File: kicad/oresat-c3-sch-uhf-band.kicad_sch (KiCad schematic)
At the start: 126 parts, among them Q3 NTR4101, Q4 PMV45EN, U16 AX5043, U18 LT5534, U19 BDCN-20-13+, U20 QPC1022, U21 TQP7M9105, U22 LT5534, U25 SN74LVC1G11IDCKRQ1, U26 TLV7041DBV, U27 LP2985AIM5-1.8_NOPB, U29 TQP3M9036, U32 SF2446E, U33 SF2446E, U40 MAX941EUA+, X1 TYKTBLSANF-16.000000

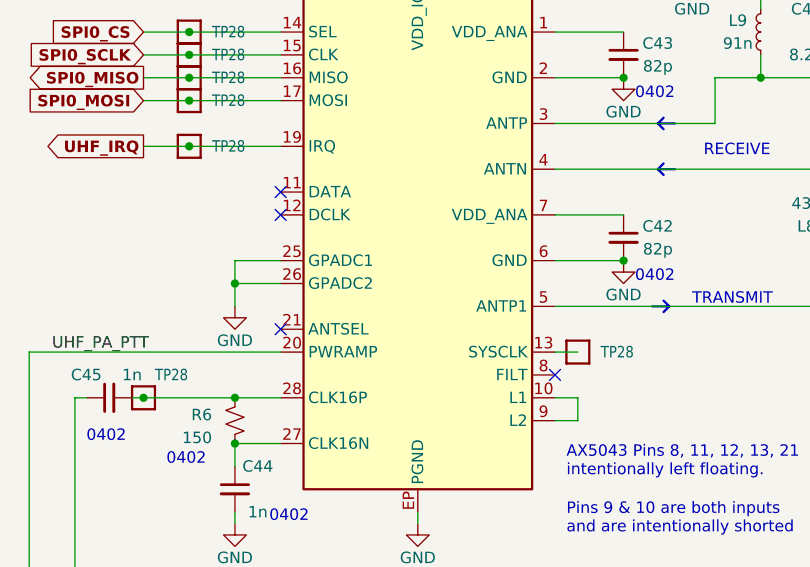
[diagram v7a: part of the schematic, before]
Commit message: Fixed some issues, including adding mrore capacitance. Also switched back to 0.38 mm for 50 ohm lines.
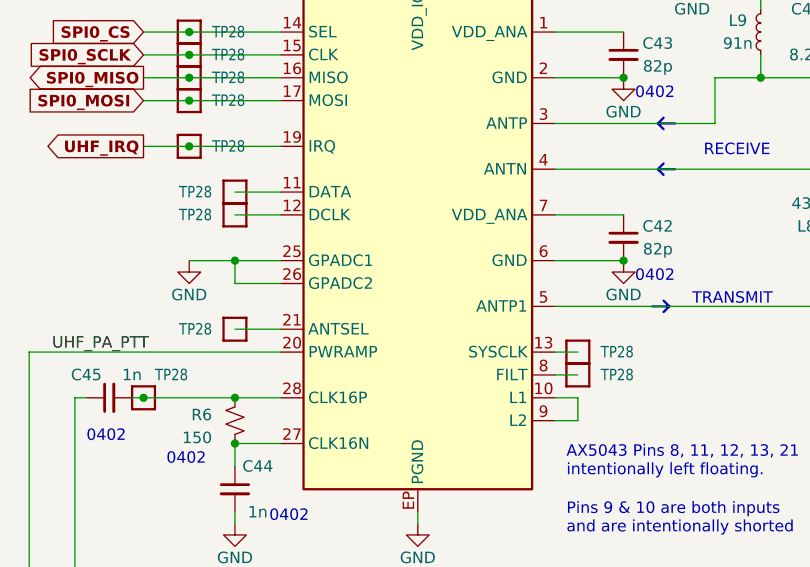
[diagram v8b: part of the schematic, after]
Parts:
- added TP28 (x4): Test-Point, oresat-misc:TestPoint_Pad_D1.0mm, symbol oresat-misc:Test-Point-1mm-round
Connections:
- net at U16.11 (DATA): now also TP28.1
- net at U16.12 (DCLK): now also TP28.1
- net at U16.21 (ANTSEL): now also TP28.1
- net at U16.8 (FILT): now also TP28.1
- no-connect marks 5 -> 1
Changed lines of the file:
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@@
   (junction (at 132.08 49.53) (diameter 0) (color 0 0 0 0)
   )
-  (junction (at 43.18 142.24) (diameter 0) (color 0 0 0 0)
-  )
   (junction (at 377.19 149.86) (diameter 0) (color 0 0 0 0)
   )
@@
   (junction (at 116.84 144.78) (diameter 0) (color 0 0 0 0)
   )
+  (junction (at 43.18 139.7) (diameter 0) (color 0 0 0 0)
+  )
   (junction (at 363.22 53.34) (diameter 0) (color 0 0 0 0)
   )
   (junction (at 38.1 119.38) (diameter 0) (color 0 0 0 0)
   )
-  (no_connect (at 48.26 132.08))
-  (no_connect (at 48.26 147.32))
-  (no_connect (at 48.26 134.62))
   (no_connect (at 30.48 215.9))
-  (no_connect (at 78.74 152.4))
   (wire (pts (xy 132.08 41.91) (xy 132.08 43.18))
     (stroke (width 0) (type default))
@@
     (stroke (width 0) (type default))
   )
+  (wire (pts (xy 43.18 132.08) (xy 48.26 132.08))
+    (stroke (width 0) (type default))
+  )
   (wire (pts (xy 96.52 48.26) (xy 96.52 46.99))
     (stroke (width 0) (type default))
@@
     (stroke (width 0) (type default))
   )
+  (wire (pts (xy 78.74 152.4) (xy 81.28 152.4))
+    (stroke (width 0) (type default))
+  )
   (wire (pts (xy 294.64 237.49) (xy 294.64 236.22))
     (stroke (width 0) (type default))
@@
     (stroke (width 0) (type default))
   )
-  (wire (pts (xy 43.18 144.78) (xy 43.18 142.24))
-    (stroke (width 0) (type default))
-  )
   (wire (pts (xy 81.28 204.47) (xy 66.04 204.47))
     (stroke (width 0) (type default))
@@
     (stroke (width 0) (type default))
   )
+  (wire (pts (xy 43.18 147.32) (xy 48.26 147.32))
+    (stroke (width 0) (type default))
+  )
   (wire (pts (xy 127 44.45) (xy 128.27 44.45))
     (stroke (width 0) (type default))
@@
     (stroke (width 0) (type default))
   )
+  (wire (pts (xy 38.1 139.7) (xy 43.18 139.7))
+    (stroke (width 0) (type default))
+  )
   (wire (pts (xy 335.28 59.69) (xy 335.28 60.96))
     (stroke (width 0) (type default))
@@
     (stroke (width 0) (type default))
   )
+  (wire (pts (xy 43.18 134.62) (xy 48.26 134.62))
+    (stroke (width 0) (type default))
+  )
   (wire (pts (xy 368.3 144.78) (xy 365.76 144.78))
     (stroke (width 0) (type default))
@@
     )
   )
+  (symbol (lib_id "oresat-misc:Test-Point-1mm-round") (at 43.18 147.32 270) (mirror x) (unit 1)
+    (in_bom yes) (on_board yes) (dnp no)
+    (property "Reference" "TP28" (at 40.64 147.3199 90)
+      (effects (font (size 1.27 1.0795)) (justify right))
+    )
+    (property "Value" "Test-Point" (at 50.8 147.32 0)
+      (effects (font (size 1.27 1.27)) hide)
+    )
+    (property "Footprint" "oresat-misc:TestPoint_Pad_D1.0mm" (at 53.34 147.32 0)
+      (effects (font (size 1.27 1.27)) hide)
+    )
+    (property "Datasheet" "" (at 43.18 147.32 0)
+      (effects (font (size 1.27 1.27)) hide)
+    )
+    (pin "1")
+    (instances
+      (project "oresat-c3"
+        (path "/65d12cdd-c326-4033-9053-c59fa4e0b25e/1b68ea4b-cacf-4529-b1d4-9be5d7c1043c"
+          (reference "TP28") (unit 1)
+        )
+        (path "/65d12cdd-c326-4033-9053-c59fa4e0b25e/05e45903-5042-4bc1-87af-e9d7510ea02d"
+          (reference "TP122") (unit 1)
+        )
+      )
+    )
+  )
   (symbol (lib_id "power:GND") (at 327.66 175.26 0) (mirror y) (unit 1)
     (in_bom yes) (on_board yes) (dnp no)
@@
     )
   )
+  (symbol (lib_id "oresat-misc:Test-Point-1mm-round") (at 43.18 134.62 270) (mirror x) (unit 1)
+    (in_bom yes) (on_board yes) (dnp no)
+    (property "Reference" "TP28" (at 40.64 134.6199 90)
+      (effects (font (size 1.27 1.0795)) (justify right))
+    )
+    (property "Value" "Test-Point" (at 50.8 134.62 0)
+      (effects (font (size 1.27 1.27)) hide)
+    )
+    (property "Footprint" "oresat-misc:TestPoint_Pad_D1.0mm" (at 53.34 134.62 0)
+      (effects (font (size 1.27 1.27)) hide)
+    )
+    (property "Datasheet" "" (at 43.18 134.62 0)
+      (effects (font (size 1.27 1.27)) hide)
+    )
+    (pin "1")
+    (instances
+      (project "oresat-c3"
+        (path "/65d12cdd-c326-4033-9053-c59fa4e0b25e/1b68ea4b-cacf-4529-b1d4-9be5d7c1043c"
+          (reference "TP28") (unit 1)
+        )
+        (path "/65d12cdd-c326-4033-9053-c59fa4e0b25e/05e45903-5042-4bc1-87af-e9d7510ea02d"
+          (reference "TP88") (unit 1)
+        )
+      )
+    )
+  )
   (symbol (lib_id "oresat-ics:AX5043") (at 63.5 137.16 0) (unit 1)
     (in_bom yes) (on_board yes) (dnp no) (fields_autoplaced)
@@
     )
   )
-  (symbol (lib_id "power:GND") (at 43.18 144.78 0) (mirror y) (unit 1)
+  (symbol (lib_id "power:GND") (at 38.1 139.7 0) (mirror y) (unit 1)
     (in_bom yes) (on_board yes) (dnp no)
-    (property "Reference" "#PWR0224" (at 43.18 151.13 0)
+    (property "Reference" "#PWR0224" (at 38.1 146.05 0)
       (effects (font (size 1.27 1.27)) hide)
     )
-    (property "Value" "GND" (at 43.18 148.59 0)
+    (property "Value" "GND" (at 38.1 143.51 0)
       (effects (font (size 1.27 1.27)))
     )
-    (property "Footprint" "" (at 43.18 144.78 0)
+    (property "Footprint" "" (at 38.1 139.7 0)
       (effects (font (size 1.27 1.27)) hide)
     )
-    (property "Datasheet" "" (at 43.18 144.78 0)
+    (property "Datasheet" "" (at 38.1 139.7 0)
       (effects (font (size 1.27 1.27)) hide)
     )
@@
     )
   )
+  (symbol (lib_id "oresat-misc:Test-Point-1mm-round") (at 43.18 132.08 270) (mirror x) (unit 1)
+    (in_bom yes) (on_board yes) (dnp no)
+    (property "Reference" "TP28" (at 40.64 132.0799 90)
+      (effects (font (size 1.27 1.0795)) (justify right))
+    )
+    (property "Value" "Test-Point" (at 50.8 132.08 0)
+      (effects (font (size 1.27 1.27)) hide)
+    )
+    (property "Footprint" "oresat-misc:TestPoint_Pad_D1.0mm" (at 53.34 132.08 0)
+      (effects (font (size 1.27 1.27)) hide)
+    )
+    (property "Datasheet" "" (at 43.18 132.08 0)
+      (effects (font (size 1.27 1.27)) hide)
+    )
+    (pin "1")
+    (instances
+      (project "oresat-c3"
+        (path "/65d12cdd-c326-4033-9053-c59fa4e0b25e/1b68ea4b-cacf-4529-b1d4-9be5d7c1043c"
+          (reference "TP28") (unit 1)
+        )
+        (path "/65d12cdd-c326-4033-9053-c59fa4e0b25e/05e45903-5042-4bc1-87af-e9d7510ea02d"
+          (reference "TP50") (unit 1)
+        )
+      )
+    )
+  )
   (symbol (lib_id "Device:L_Small") (at 234.95 218.44 0) (unit 1)
     (in_bom yes) (on_board yes) (dnp no)
@@
         )
       )
+    )
+  )
+  (symbol (lib_id "oresat-misc:Test-Point-1mm-round") (at 81.28 152.4 0) (unit 1)
+    (in_bom yes) (on_board yes) (dnp no) (fields_autoplaced)
+    (property "Reference" "TP28" (at 83.82 152.4 0)
+      (effects (font (size 1.27 1.0795)) (justify left))
+    )
+    (property "Value" "Test-Point" (at 81.28 144.78 0)
+      (effects (font (size 1.27 1.27)) hide)
+    )
+    (property "Footprint" "oresat-misc:TestPoint_Pad_D1.0mm" (at 81.28 142.24 0)
+      (effects (font (size 1.27 1.27)) hide)
+    )
+    (property "Datasheet" "" (at 81.28 152.4 0)
+      (effects (font (size 1.27 1.27)) hide)
+    )
+    (pin "1")
+    (instances
+      (project "oresat-c3"
+        (path "/65d12cdd-c326-4033-9053-c59fa4e0b25e/1b68ea4b-cacf-4529-b1d4-9be5d7c1043c"
+          (reference "TP28") (unit 1)
+        )
+        (path "/65d12cdd-c326-4033-9053-c59fa4e0b25e/05e45903-5042-4bc1-87af-e9d7510ea02d"
+          (reference "TP89") (unit 1)
+        )
+      )
